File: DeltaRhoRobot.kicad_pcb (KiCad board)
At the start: 4 copper layers, 75 x 100 mm, 135 parts, among them J1 Conn_01x02_Socket, J10 Conn_01x02, J11 Conn_01x08, J12 USB_C_Receptacle_USB2.0, J13 Conn_02x09_Top_Bottom, J14 Conn_01x09, J15 Conn_02x09_Top_Bottom, J2 USB_C_Receptacle_USB2.0, J3 USB_C_Receptacle_USB2.0, J4 JST-XH, J5 JST-XH, J6 Conn_01x09, J7 Conn_02x20_Counter_Clockwise, P1 B6B-ZRLFSN, P2 B6B-ZRLFSN, P3 B6B-ZRLFSN, P4 B6B-ZRLFSN, P5 B6B-ZRLFSN, P6 B6B-ZRLFSN, Q2 BSS138, Q5 BSS138, SW1 CAS-120A1, SW4 SW_Push, U10 ICM-42688-P, U11 LIS3MDL, U12 ESP32-CAM, U13 MIC5365-3.3YC5, U14 W25Q16JVS, U2 AMS1117-3.3, U3 DRV8835DSSR, U4 RP2040, U5 DRV8835DSSR, U6 DRV8835DSSR, U7 TPS566242DRLR, U8 ESP32-S3-WROOM-1-N8R2, U9 FT231XQ, Y1 ABM8-272-T3

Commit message: Rev 2 finished
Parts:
- R10, R3: footprint Resistor_SMD:R_0402_1005Metric -> Resistor_SMD:R_0603_1608Metric
- moved C4 0.57 mm to (170.8, 78.4)
- moved C3 0.14 mm to (172.0, 90.5)
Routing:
- net +5V: track 174.2 -> 168.8 mm
- net Earth: track 216.4 -> 218.9 mm
- net VCC: track 127.5 -> 125.1 mm
- net /Pico/M3_Enc_A: track 32.0 -> 32.8 mm
- net Pico_SCL1: track 80.1 -> 80.8 mm

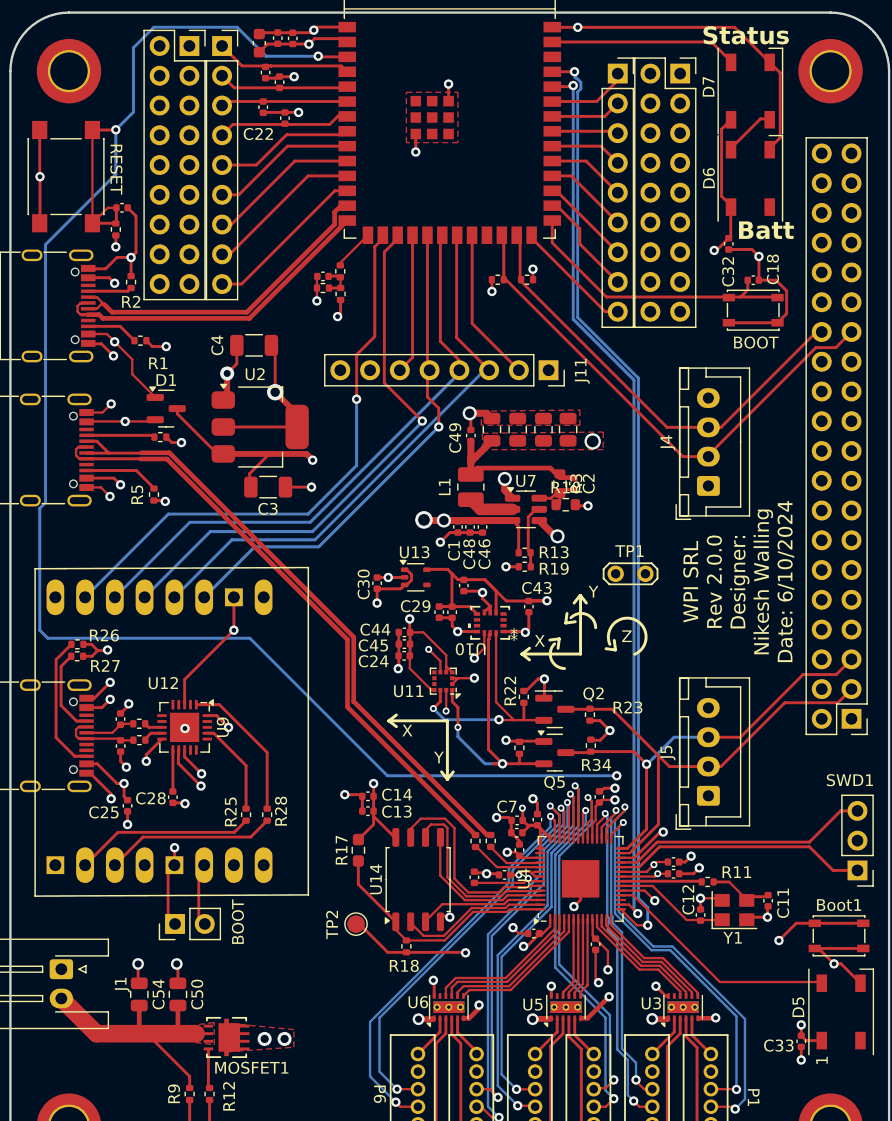
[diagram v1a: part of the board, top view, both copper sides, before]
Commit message: Rev 3: fixing I2C and footprints
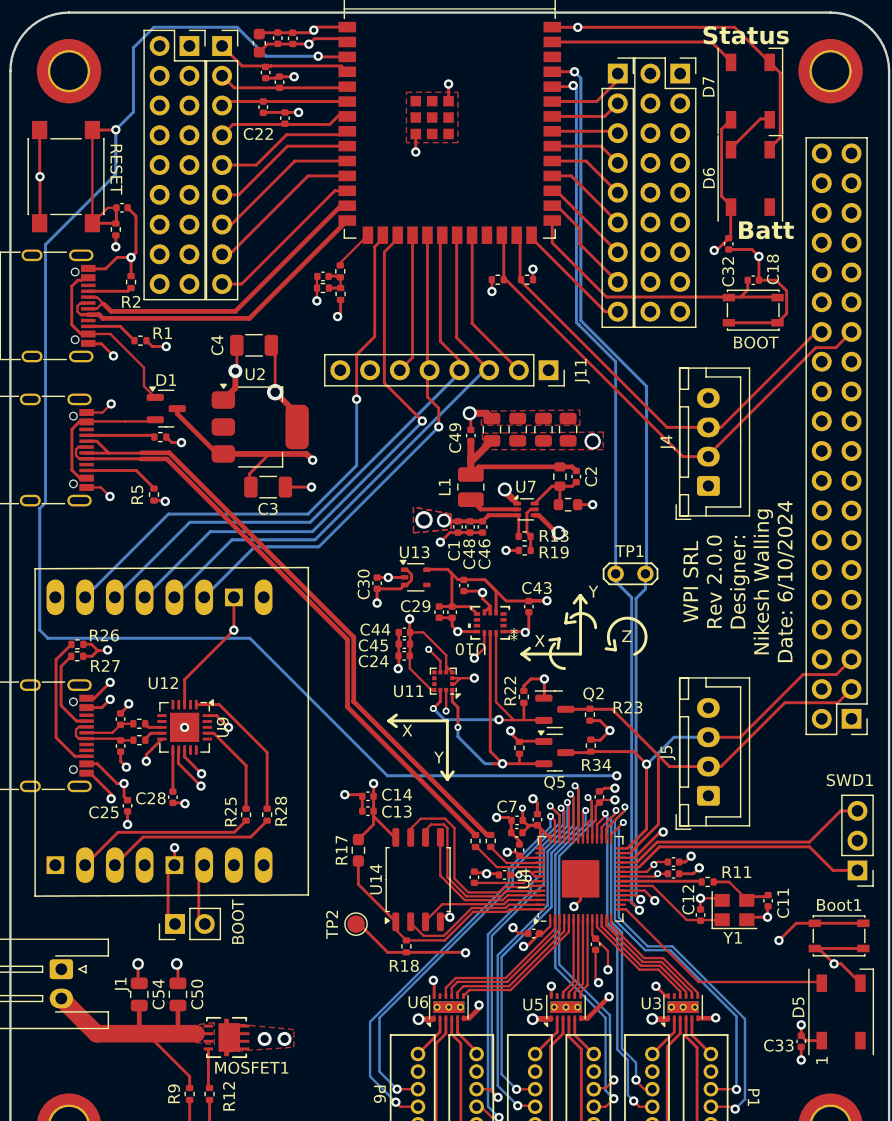
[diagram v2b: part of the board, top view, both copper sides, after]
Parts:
- R15: value 27 -> 33
- U13: value MIC5365-3.3YC5 -> MIC5366-1.8YC5-TR
- U7: footprint Package_TO_SOT_SMD:SOT-23-6 -> Package_TO_SOT_SMD:SOT-563
- moved R13 1.39 mm to (193.9, 94.7)
- moved R19 1.39 mm to (193.9, 95.9)
- moved C2 0.63 mm to (198.3, 89.6)
- moved R3 0.60 mm to (196.9, 89.6)
- moved R10 0.20 mm to (197.6, 92.0)
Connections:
- R15 pad 1: /Pico/USB_DP_Pico -> /Pico/USB_DM_Pico
- R16 pad 1: /Pico/USB_DM_Pico -> Net-(U4-USB_DM)
- R16 pad 2: Net-(U4-USB_DM) -> /Pico/USB_DP_Pico
- U4 pad 15: Pico_SCL1 -> Net-(D5-DIN)
- U4 pad 16: Pico_SDA1 -> unconnected-(U4-GPIO13-Pad16)
- U4 pad 17: unconnected-(U4-GPIO14-Pad17) -> Pico_SDA1
- U4 pad 18: Net-(D5-DIN) -> Pico_SCL1
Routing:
- net +3.3V: track 86.7 -> 80.4 mm
- net Pico_SCL1: track 80.8 -> 77.5 mm
- net /V_USB_2: track 14.6 -> 12.4 mm, vias 2 -> 0
- net VCC: track 125.1 -> 123.4 mm
- net Net-(U7-FB): track 4.52 -> 6.01 mm
- net Earth: track 218.9 -> 220.2 mm
- net Net-(U7-EN): track 5.24 -> 4.21 mm
- net /ESP_USB_D-: track 28.1 -> 27.4 mm
- net /V_USB_1: track 16.2 -> 15.7 mm, vias 2 -> 0
- net +1V8: track 59.3 -> 58.8 mm

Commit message: Cleaning up
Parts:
- R11: value R_US -> 1k
- R16: value 27 -> 33
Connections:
- R15 pad 1: /Pico/USB_DM_Pico -> /Pico/USB_DP_Pico
- R16 pad 1: Net-(U4-USB_DM) -> /Pico/USB_DM_Pico
- R16 pad 2: /Pico/USB_DP_Pico -> Net-(U4-USB_DM)
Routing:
- net Earth: track 220.2 -> 203.3 mm
- net +5V: track 168.8 -> 175.2 mm
- net +3.3V: track 80.4 -> 85.9 mm
- net /ESP_PU: track 154.5 -> 155.3 mm
- net Net-(J10-Pin_2): track 4.97 -> 4.44 mm

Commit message: Progress
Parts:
- P1, P2, P3, P4, P5, P6: footprint JST-ZR:CONN_B6B-ZR_JST -> B6B-ZR:CONN_B6B-ZR_JST
- SW1: footprint switch185:1825232-1_TEC -> Switch185:1825232-1_TEC
- moved SW4 175.6 mm to (44.0, 121.8)
- moved C32 163.2 mm to (64.2, 140.5), turned to 0 degrees
- moved C43 151.3 mm to (51.3, 150.3), turned to 0 degrees
- moved C31 146.0 mm to (51.3, 148.3), turned to 0 degrees
- moved Q5 145.1 mm to (55.2, 146.5)
- moved Q2 144.9 mm to (55.2, 141.9)
- moved R34 144.5 mm to (59.1, 146.4), turned to 0 degrees
- moved R23 144.1 mm to (59.1, 142.5), turned to 0 degrees
- moved C29 142.0 mm to (51.3, 144.4), turned to 0 degrees
- moved C23 141.9 mm to (51.3, 140.5), turned to 0 degrees
- moved C45 141.6 mm to (51.3, 154.3)
- moved C44 141.2 mm to (51.3, 152.3), turned to 0 degrees
- moved R22 138.5 mm to (59.1, 140.5), turned to 0 degrees
- moved C30 138.4 mm to (51.3, 146.4), turned to 0 degrees
- moved R33 138.0 mm to (59.1, 144.5), turned to 0 degrees
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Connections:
- J14 pad 1: /ESP32-S3-WROOM-1/GPIO42 -> /ESP32-S3-WROOM-1/GPIO_2
- J14 pad 2: /ESP32-S3-WROOM-1/GPIO41 -> /ESP32-S3-WROOM-1/GPIO_43
- J14 pad 3: /ESP32-S3-WROOM-1/GPIO40 -> /ESP32-S3-WROOM-1/GPIO_44
- J14 pad 4: /ESP32-S3-WROOM-1/GPIO39 -> /ESP32-S3-WROOM-1/GPIO42
- J14 pad 5: /ESP32-S3-WROOM-1/GPIO38 -> /ESP32-S3-WROOM-1/GPIO41
- J14 pad 6: /ESP32-S3-WROOM-1/GPIO37 -> /ESP32-S3-WROOM-1/GPIO40
- J14 pad 7: /ESP32-S3-WROOM-1/GPIO36 -> /ESP32-S3-WROOM-1/GPIO39
- J14 pad 8: /ESP32-S3-WROOM-1/GPIO35 -> /ESP32-S3-WROOM-1/GPIO38
- J14 pad 9: /ESP32-S3-WROOM-1/GPIO45 -> /ESP32-S3-WROOM-1/GPIO37
- J4 pad 2: /ESP32-S3-WROOM-1/SDA -> Pico_SDA1
- J4 pad 3: /ESP32-S3-WROOM-1/SCL -> Pico_SCL1
- J7 pad 27: /ESP32-S3-WROOM-1/SDA -> /ESP32-S3-WROOM-1/TWI_SDA
- J7 pad 28: /ESP32-S3-WROOM-1/SCL -> /ESP32-S3-WROOM-1/TWI_SCL
- R20 pad 2: /ESP32-S3-WROOM-1/SDA -> Pico_SDA1
- R21 pad 2: /ESP32-S3-WROOM-1/SCL -> Pico_SCL1
- U8 pad 23: /ESP32-S3-WROOM-1/ESP_CS2 -> Pico_SCL1
- U8 pad 24: /ESP32-S3-WROOM-1/SDA -> Pico_SDA1
- U8 pad 25: /ESP32-S3-WROOM-1/SCL -> /ESP32-S3-WROOM-1/TWI_SDA
- U8 pad 26: /ESP32-S3-WROOM-1/GPIO45 -> /ESP32-S3-WROOM-1/TWI_SCL
- U8 pad 36: Pico_SDA1 -> /ESP32-S3-WROOM-1/GPIO_44
- U8 pad 37: Pico_SCL1 -> /ESP32-S3-WROOM-1/GPIO_43
- U8 pad 38: unconnected-(U8-GPIO2/TOUCH2/ADC1_CH1-Pad38) -> /ESP32-S3-WROOM-1/GPIO_2
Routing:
- net +5V: track 175.2 -> 9.93 mm, vias 4 -> 0
- net Earth: track 203.3 -> 49.0 mm, vias 63 -> 26
- net /ESP_PU: track 155.3 -> 1.96 mm, vias 4 -> 1
- net VCC: track 123.2 -> 9.14 mm, vias 8 -> 2
- net Pico_SCL1: track 77.3 -> 0.00 mm, vias 2 -> 0
- net Pico_SDA1: track 76.5 -> 0.00 mm, vias 2 -> 0
- net +3.3V: track 85.9 -> 10.1 mm, vias 18 -> 2
- net +1V8: track 58.7 -> 0.00 mm, vias 5 -> 0
- net /Pico/USB_DM_Pico: track 53.4 -> 2.76 mm
- net /Pico/USB_DP_Pico: track 52.3 -> 2.87 mm
- net /ESP32-S3-WROOM-1/ESP_SCLK: track 48.3 -> 0.00 mm
- net /ESP32-S3-WROOM-1/Handshake: track 47.8 -> 0.00 mm, vias 1 -> 0
- net /ESP32-S3-WROOM-1/ESP_CS1: track 47.3 -> 0.00 mm, vias 1 -> 0
- net /ESP32-S3-WROOM-1/ESP_MISO: track 47.1 -> 0.00 mm
- net /ESP32-S3-WROOM-1/SDA: track 43.6 -> 0.00 mm
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- added copper zone on In2.Cu, net VCC
- removed copper zone on In2.Cu, net +5V
- removed copper zone on F.Cu, net Earth
- removed copper zone on F.Cu, net VIN
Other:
- board size 75 x 100 mm -> 80 x 80 mm
- board text removed: "Batt"
- board text removed: "Status"
- board text removed: "WPI SRL Rev 2.0.0 Designer: Nikesh Walling Date: 6/10/2024"
- board text removed: "X"
- board text removed: "Y"
- board text removed: "Z"

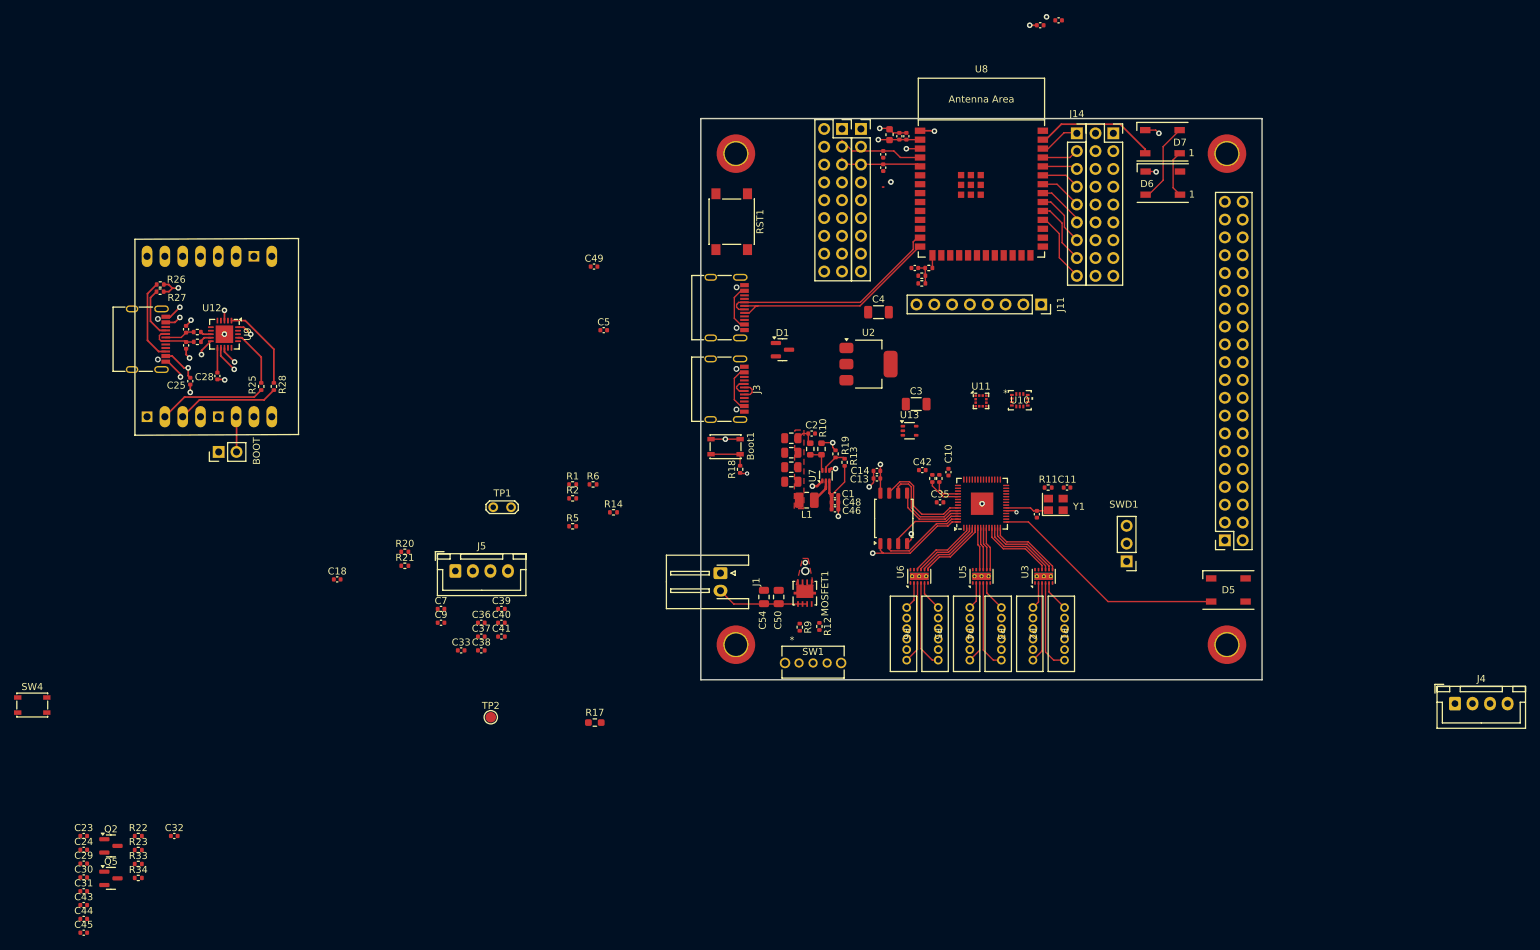
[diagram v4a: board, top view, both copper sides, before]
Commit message: Layout for 80x80mm done
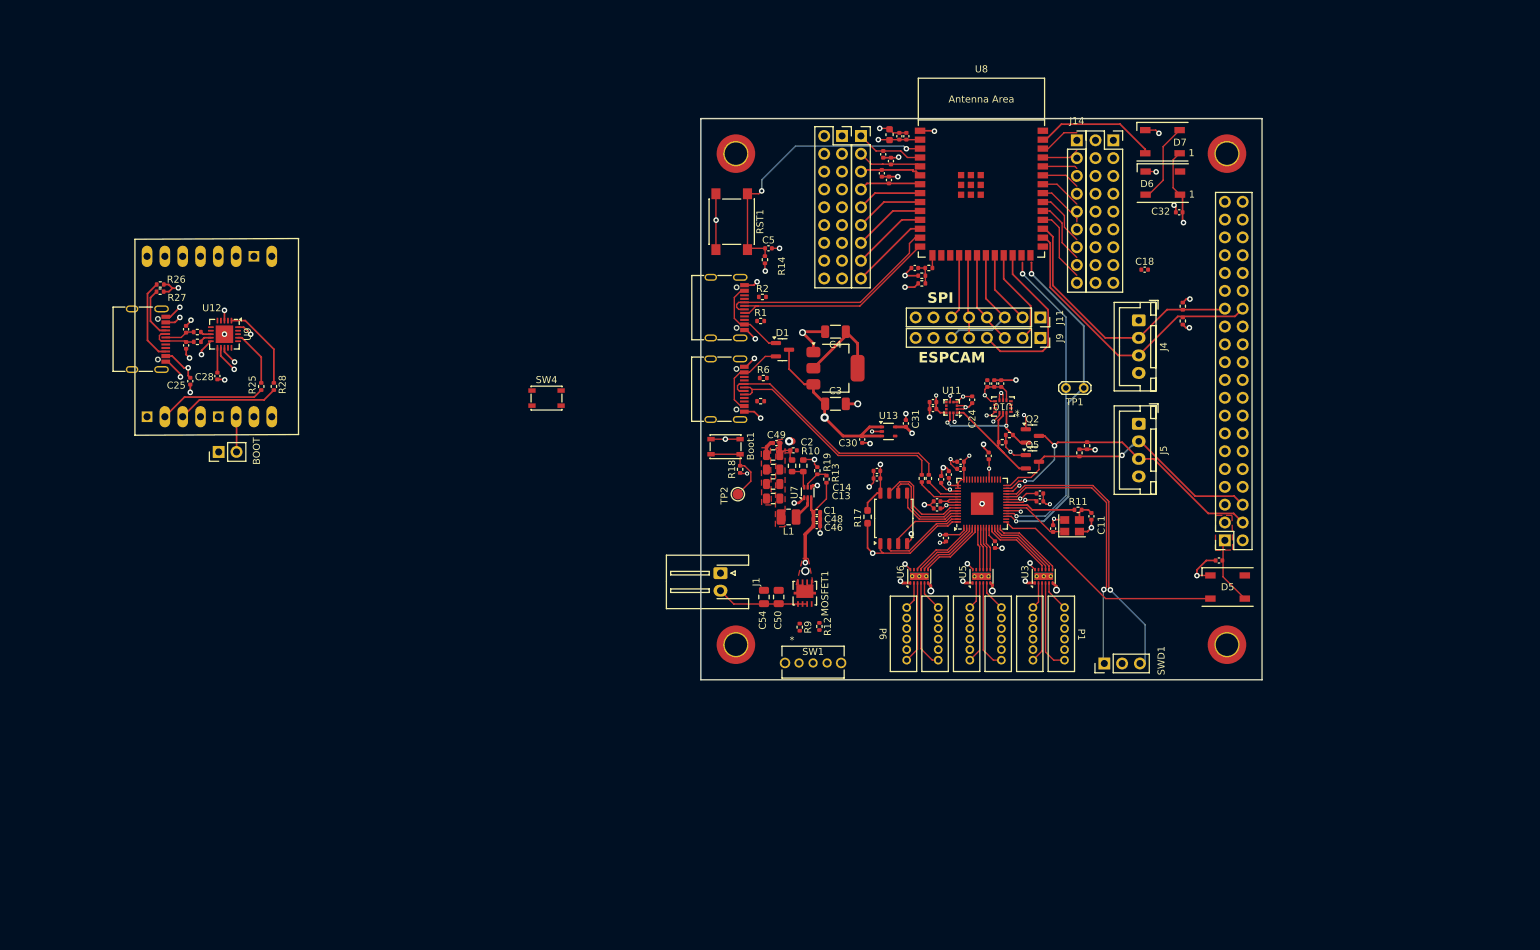
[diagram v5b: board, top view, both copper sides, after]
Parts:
- added J9: Conn_01x08, Connector_PinSocket_2.54mm:PinSocket_1x08_P2.54mm_Vertical, F.Cu at (187.7, 69.5)
- moved C32 168.6 mm to (207.5, 51.6)
- moved C43 149.6 mm to (181.1, 76.0), turned to 90 degrees
- moved C29 147.6 mm to (182.1, 76.0), turned to -90 degrees
- moved R34 147.2 mm to (193.3, 85.9), turned to -90 degrees
- moved R23 147.0 mm to (194.4, 84.8), turned to 90 degrees
- moved Q5 144.2 mm to (186.6, 87.1)
- moved C23 144.0 mm to (180.1, 76.0), turned to 90 degrees
- moved Q2 143.8 mm to (186.6, 83.4)
- moved C45 142.7 mm to (172.4, 78.6)
- moved C24 142.0 mm to (178.0, 78.3), turned to -90 degrees
- moved C44 141.2 mm to (172.4, 79.6), turned to 180 degrees
- moved R33 137.0 mm to (182.3, 84.3), turned to 180 degrees
- moved R22 136.7 mm to (183.3, 83.3)
- moved C31 134.8 mm to (168.5, 81.7), turned to 90 degrees
- moved C30 127.3 mm to (162.3, 83.9), turned to -90 degrees
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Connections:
- C30 pad 1: +3.3V -> +5V
- J4 pad 2: Pico_SDA1 -> /ESP32-S3-WROOM-1/SCL
- J4 pad 3: Pico_SCL1 -> /ESP32-S3-WROOM-1/SDA
- J5 pad 2: PICO_SDA -> PICO_SCL
- J5 pad 3: PICO_SCL -> PICO_SDA
- J7 pad 1: unconnected-(J7-Pin_1-Pad1) -> +5V
- J7 pad 10: unconnected-(J7-Pin_10-Pad10) -> Earth
- J7 pad 2: +5V -> unconnected-(J7-Pin_2-Pad2)
- J7 pad 25: Earth -> unconnected-(J7-Pin_25-Pad25)
- J7 pad 26: unconnected-(J7-Pin_26-Pad26) -> Earth
- J7 pad 27: /ESP32-S3-WROOM-1/TWI_SDA -> /ESP32-S3-WROOM-1/SCL
- J7 pad 28: /ESP32-S3-WROOM-1/TWI_SCL -> /ESP32-S3-WROOM-1/SDA
- J7 pad 3: PICO_SDA -> +5V
- J7 pad 39: Earth -> unconnected-(J7-Pin_39-Pad39)
- J7 pad 4: +5V -> PICO_SDA
- J7 pad 40: unconnected-(J7-Pin_40-Pad40) -> Earth
- J7 pad 5: PICO_SCL -> Earth
- J7 pad 6: Earth -> PICO_SCL
- J7 pad 9: Earth -> unconnected-(J7-Pin_9-Pad9)
- R20 pad 2: Pico_SDA1 -> /ESP32-S3-WROOM-1/SCL
- R21 pad 2: Pico_SCL1 -> /ESP32-S3-WROOM-1/SDA
- U13 pad 1: +3.3V -> +5V
- U13 pad 3: +3.3V -> +5V
- U8 pad 16: /ESP32-S3-WROOM-1/Handshake -> /ESP32-S3-WROOM-1/ESP_CS2
- U8 pad 17: /ESP32-S3-WROOM-1/ESP_CS1 -> unconnected-(U8-GPIO9/TOUCH9/ADC1_CH8/FSPIHD/SUBSPIHD-Pad17)
- U8 pad 23: Pico_SCL1 -> /ESP32-S3-WROOM-1/Handshake
- U8 pad 24: Pico_SDA1 -> /ESP32-S3-WROOM-1/ESP_CS1
- U8 pad 25: /ESP32-S3-WROOM-1/TWI_SDA -> Pico_SDA1
- U8 pad 26: /ESP32-S3-WROOM-1/TWI_SCL -> Pico_SCL1
- U8 pad 28: /ESP32-S3-WROOM-1/GPIO35 -> /ESP32-S3-WROOM-1/SDA
- U8 pad 29: /ESP32-S3-WROOM-1/GPIO36 -> /ESP32-S3-WROOM-1/SCL
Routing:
- net +5V: track 9.93 -> 160.3 mm, vias 0 -> 3
- net Earth: track 49.0 -> 132.3 mm, vias 26 -> 57
- net +3.3V: track 10.1 -> 67.9 mm, vias 2 -> 16
- net Pico_SDA1: track 0.00 -> 48.0 mm, vias 0 -> 2
- net Pico_SCL1: track 0.00 -> 45.7 mm, vias 0 -> 2
- net PICO_SDA: track 0.00 -> 45.1 mm, vias 0 -> 2
- net VCC: track 9.14 -> 52.3 mm, vias 2 -> 6
- net /ESP32-S3-WROOM-1/SDA: track 0.00 -> 42.1 mm
- net /Pico/SWD: track 0.00 -> 41.3 mm, vias 0 -> 1
- net PICO_SCL: track 0.00 -> 40.7 mm, vias 0 -> 1
- net /ESP_PU: track 1.96 -> 42.4 mm, vias 1 -> 3
- net /Pico/SWCLK: track 0.00 -> 38.9 mm, vias 0 -> 1
- net /ESP32-S3-WROOM-1/SCL: track 0.00 -> 38.4 mm
- net /Pico/USB_DM_Pico: track 2.76 -> 35.3 mm
- net /Pico/USB_DP_Pico: track 2.87 -> 33.3 mm
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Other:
- board text added: "ESPCAM"
- board text added: "SPI"

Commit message: Finished new board
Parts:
- removed C18, C28: 100nF, Capacitor_SMD:C_0402_1005Metric
- removed C25: 10uF, Capacitor_SMD:C_0402_1005Metric
- removed C26, C27: 47pF, Capacitor_SMD:C_0402_1005Metric
- removed J10: Conn_01x02, Connector_PinHeader_2.54mm:PinHeader_1x02_P2.54mm_Vertical
- removed J12: USB_C_Receptacle_USB2.0, Connector_USB:USB_C_Receptacle_G-Switch_GT-USB-7010ASV
- removed R25, R28: 0, Resistor_SMD:R_0402_1005Metric
- removed R26, R27: 5K, Resistor_SMD:R_0402_1005Metric
- removed R29, R30: 33, Resistor_SMD:R_0402_1005Metric
- removed SW4: SW_Push, Button_Switch_SMD:SW_SPST_PTS810
- removed U12: ESP32-CAM, ESP32CAM:ESP32-CAM
- removed U9: FT231XQ, Package_DFN_QFN:QFN-20-1EP_4x4mm_P0.5mm_EP2.5x2.5mm
- moved D5 17.2 mm to (197.5, 108.4), turned to 90 degrees
- moved SWD1 16.8 mm to (198.0, 99.2), turned to 180 degrees
- moved C33 14.9 mm to (198.6, 104.2), turned to 180 degrees
- moved R20 14.4 mm to (194.0, 68.3), turned to 90 degrees
- moved R21 14.4 mm to (194.0, 70.4), turned to -90 degrees
- moved H3 11.2 mm to (204.3, 108.2)
- moved J7 10.4 mm to (203.8, 99.9)
- moved C32 10.3 mm to (197.8, 55.0)
- moved H2 10.0 mm to (204.3, 43.2)
- moved C4 8.81 mm to (164.5, 75.0), turned to 90 degrees
- moved D6 8.06 mm to (197.9, 51.0), turned to -90 degrees
- moved J4 7.76 mm to (197.5, 73.5), turned to 90 degrees
- moved D7 7.48 mm to (197.9, 43.6), turned to 90 degrees
- moved J5 6.94 mm to (197.5, 87.2), turned to 90 degrees
- moved C12 5.53 mm to (190.8, 91.3), turned to 0 degrees
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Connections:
- J4 pad 1: +5V -> Earth
- J4 pad 2: /ESP32-S3-WROOM-1/SCL -> /ESP32-S3-WROOM-1/SDA
- J4 pad 3: /ESP32-S3-WROOM-1/SDA -> /ESP32-S3-WROOM-1/SCL
- J4 pad 4: Earth -> +5V
- J5 pad 1: +5V -> Earth
- J5 pad 2: PICO_SCL -> PICO_SDA
- J5 pad 3: PICO_SDA -> PICO_SCL
- J5 pad 4: Earth -> +5V
- U4 pad 38: /Pico/M5_Enc_A -> /Pico/M5_Enc_B
- U4 pad 39: /Pico/M5_Enc_B -> /Pico/M5_Enc_A
- U4 pad 40: /Pico/M6_Enc_A -> /Pico/M6_Enc_B
- U4 pad 41: /Pico/M6_Enc_B -> /Pico/M6_Enc_A
- U8 pad 25: Pico_SDA1 -> Pico_SCL1
- U8 pad 26: Pico_SCL1 -> Pico_SDA1
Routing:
- net /ESP_PU: track 42.4 -> 93.3 mm, vias 3 -> 4
- net VCC: track 52.3 -> 95.0 mm
- net /Pico/M1_Enc_B: track 0.00 -> 32.7 mm, vias 0 -> 1
- net /Pico/M6_Enc_B: track 0.00 -> 32.6 mm, vias 0 -> 1
- net /Pico/M4_Enc_B: track 0.00 -> 32.1 mm, vias 0 -> 1
- net /Pico/M5_Enc_B: track 0.00 -> 31.9 mm, vias 0 -> 1
- net /Pico/M6_Enc_A: track 0.00 -> 31.8 mm, vias 0 -> 1
- net /Pico/M2_Enc_B: track 0.00 -> 30.4 mm, vias 0 -> 1
- net /Pico/M1_Enc_A: track 0.00 -> 30.0 mm, vias 0 -> 1
- net /Pico/M2_Enc_A: track 0.00 -> 29.6 mm, vias 0 -> 1
- net /Pico/M4_Enc_A: track 0.00 -> 29.3 mm, vias 0 -> 1
- net /Pico/M3_Enc_B: track 0.00 -> 28.3 mm, vias 0 -> 1
- net /Pico/M5_Enc_A: track 0.00 -> 28.1 mm, vias 0 -> 1
- net /Pico/M3_Enc_A: track 0.00 -> 28.0 mm, vias 0 -> 1
- net /ESP32-S3-WROOM-1/ESP32CAM/V_USB: track 25.7 -> 0.00 mm, vias 3 -> 0
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- added copper zone on In2.Cu, net +5V
- added copper zone on F.Cu, net Earth
- added copper zone on F.Cu, net VIN
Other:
- board size 80 x 80 mm -> 70 x 75 mm
- board text added: "Batt"

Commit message: Cleaning
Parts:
- J1: footprint Connector_JST:JST_XH_S2B-XH-A-1_1x02_P2.50mm_Horizontal -> Connector_JST:JST_XH_B2B-XH-A_1x02_P2.50mm_Vertical
- moved J1 2.15 mm to (142.5, 100.5), turned to 90 degrees
- moved D6 0.09 mm to (197.9, 51.0)
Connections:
- J1 pad 1: Earth -> VIN
- J1 pad 2: VIN -> Earth
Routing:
- net /ESP32-S3-WROOM-1/ESP_CS1: track 25.0 -> 14.2 mm, vias 0 -> 1
- net VCC: track 95.0 -> 93.3 mm
- net /Pico/Motor_2_A: track 10.9 -> 9.74 mm
- net /ESP_USB_D-: track 27.6 -> 28.3 mm
- net /ESP_USB_D+: track 25.7 -> 26.2 mm
- net (no net): vias 1 -> 0
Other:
- board text added: "Off"
- board text added: "On"
